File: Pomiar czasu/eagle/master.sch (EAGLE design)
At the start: 36 parts, among them IC1 MEGA8-AI, IC2 lm33, U2 RFM69HW

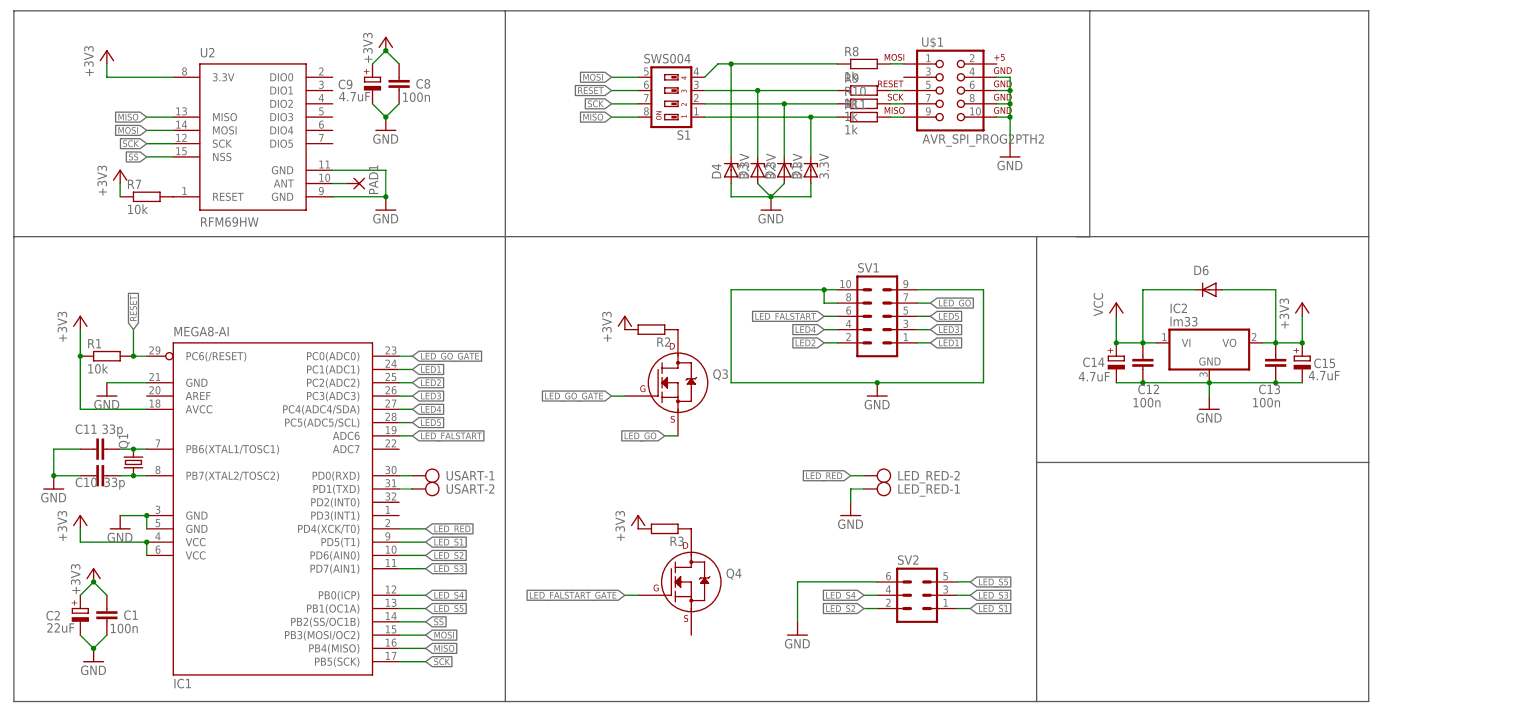
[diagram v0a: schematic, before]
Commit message: ADC slave, master project  created
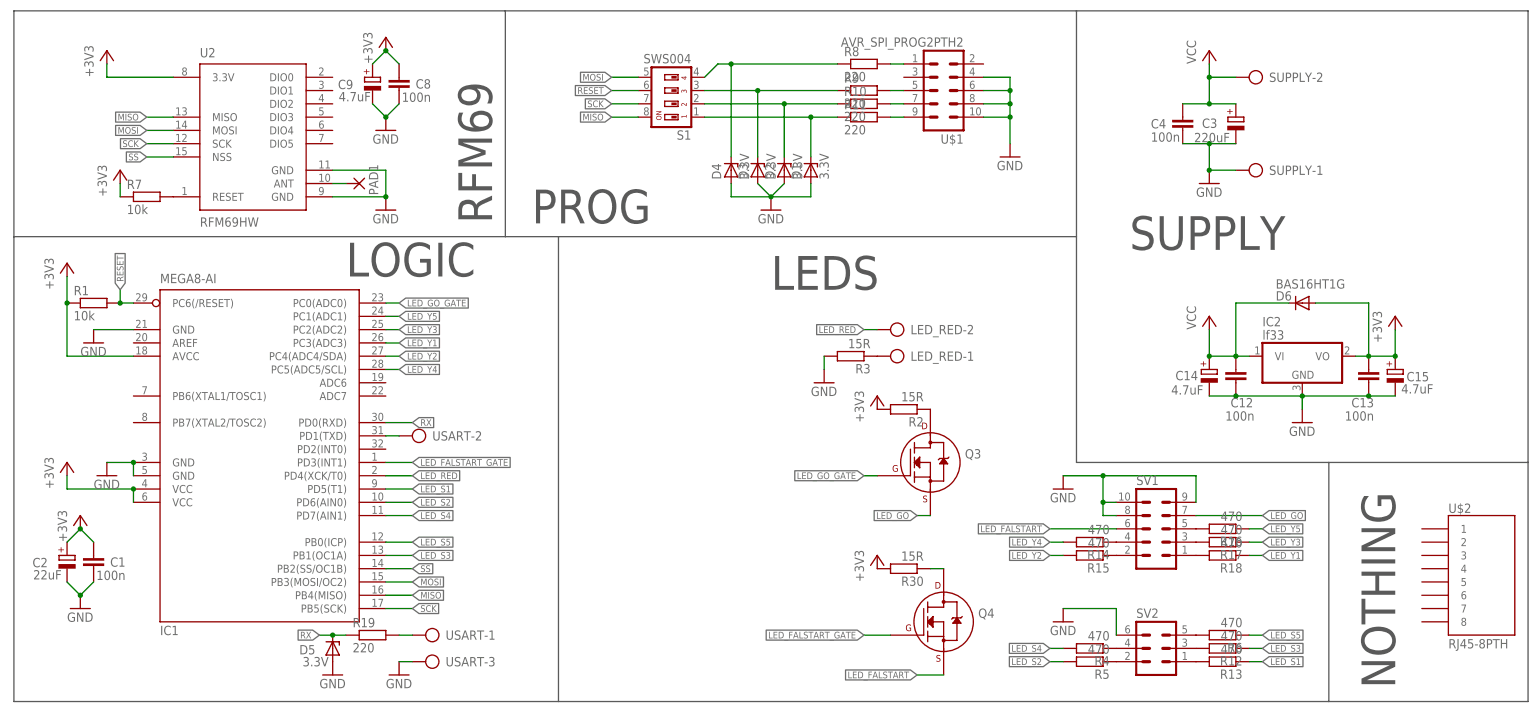
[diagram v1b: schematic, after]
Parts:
- removed C10, C11: 33p, rcl:C-EUC0805
- removed Q1: (no value), crystal:CRYSTALHC49UP
- added C3: 220uF, rcl:CPOL-EUE2-5
- added C4: 100n, rcl:C-EUC0805
- added D5: 3.3V, diode:ZENER-DIODESOD80C
- added R12, R13, R14, R15, R16, R17, R18, R4, R5, R6: 470, rcl:R-EU_R0805
- added R19: 220, rcl:R-EU_R0805
- added R30: 15R, rcl:R-EU_R0805
- added SUPPLY: (no value), con-ptr500:AK500/2
- added U$2: RJ45-8PTH, SparkFun:RJ45-8PTH
- D6: value (none) -> BAS16HT1G
- IC2: value lm33 -> lf33
- R10, R11, R8, R9: value 1k -> 220
- R2, R3: value (none) -> 15R
- U$1: device SparkFun:AVR_SPI_PROG2PTH2 -> con-harting-ml:ML10L
- USART: device con-ptr500:AK500/2 -> con-ptr500:AK500/3
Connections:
- removed net LED1: IC1.PC1(ADC1), SV1.1
- removed net LED2: IC1.PC2(ADC2), SV1.2
- removed net LED3: IC1.PC3(ADC3), SV1.3
- removed net LED4: IC1.PC4(ADC4/SDA), SV1.4
- removed net LED5: IC1.PC5(ADC5/SCL), SV1.5
- removed net N$17: C11.2, IC1.PB6(XTAL1/TOSC1), Q1.2
- removed net N$18: C10.2, IC1.PB7(XTAL2/TOSC2), Q1.1
- removed net RXD: IC1.PD0(RXD), USART-1.KL
- new net LED_Y1: IC1.PC3(ADC3), R18.1
- new net LED_Y2: IC1.PC4(ADC4/SDA), R15.2
- new net LED_Y3: IC1.PC2(ADC2), R17.1
- new net LED_Y4: IC1.PC5(ADC5/SCL), R14.2
- new net LED_Y5: IC1.PC1(ADC1), R16.1
- new net N$19: R12.2, SV2.3
- new net N$20: R13.2, SV2.1
- new net N$21: R14.1, SV1.4
- new net N$22: R15.1, SV1.2
- new net N$23: R16.2, SV1.5
- new net N$24: R17.2, SV1.3
- new net N$25: R18.2, SV1.1
- new net N$26: R19.2, USART-1.KL
- new net N$3: LED_RED-1.KL, R3.1
- new net N$4: R4.1, SV2.4
- new net N$5: R5.1, SV2.2
- new net N$6: R6.2, SV2.5
- new net RX: D5.C, IC1.PD0(RXD), R19.1
- net +3V3: now also R30.2; no longer R3.2
- net GND: now also C3.-, C4.2, D5.A, R3.2, SUPPLY-1.KL, USART-3.KL; no longer C10.1, C11.1, LED_RED-1.KL
- net LED_FALSTART: now also Q4.S; no longer IC1.ADC6
- net LED_FALSTART_GATE: now also IC1.PD3(INT1)
- net LED_S1: now also R13.1; no longer SV2.1
- net LED_S2: now also R5.2; no longer SV2.2
- net LED_S3: now also IC1.PB1(OC1A), R12.1; no longer IC1.PD7(AIN1), SV2.3
- net LED_S4: now also IC1.PD7(AIN1), R4.2; no longer IC1.PB0(ICP), SV2.4
- net LED_S5: now also IC1.PB0(ICP), R6.1; no longer IC1.PB1(OC1A), SV2.5
- net N$2: now also R30.1; no longer R3.1
- net VCC: now also C3.+, C4.1, SUPPLY-2.KL
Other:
- note added: "LEDS"
- note added: "LOGIC"
- note added: "NOTHING"
- note added: "PROG"
- note added: "RFM69"
- note added: "SUPPLY"
- moved on the sheet: C1, C12, C13, C14, C15, C2, D6, IC1, IC2, LED_RED-1, LED_RED-2, Q3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

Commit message: Slave->ctc, tsal modulation
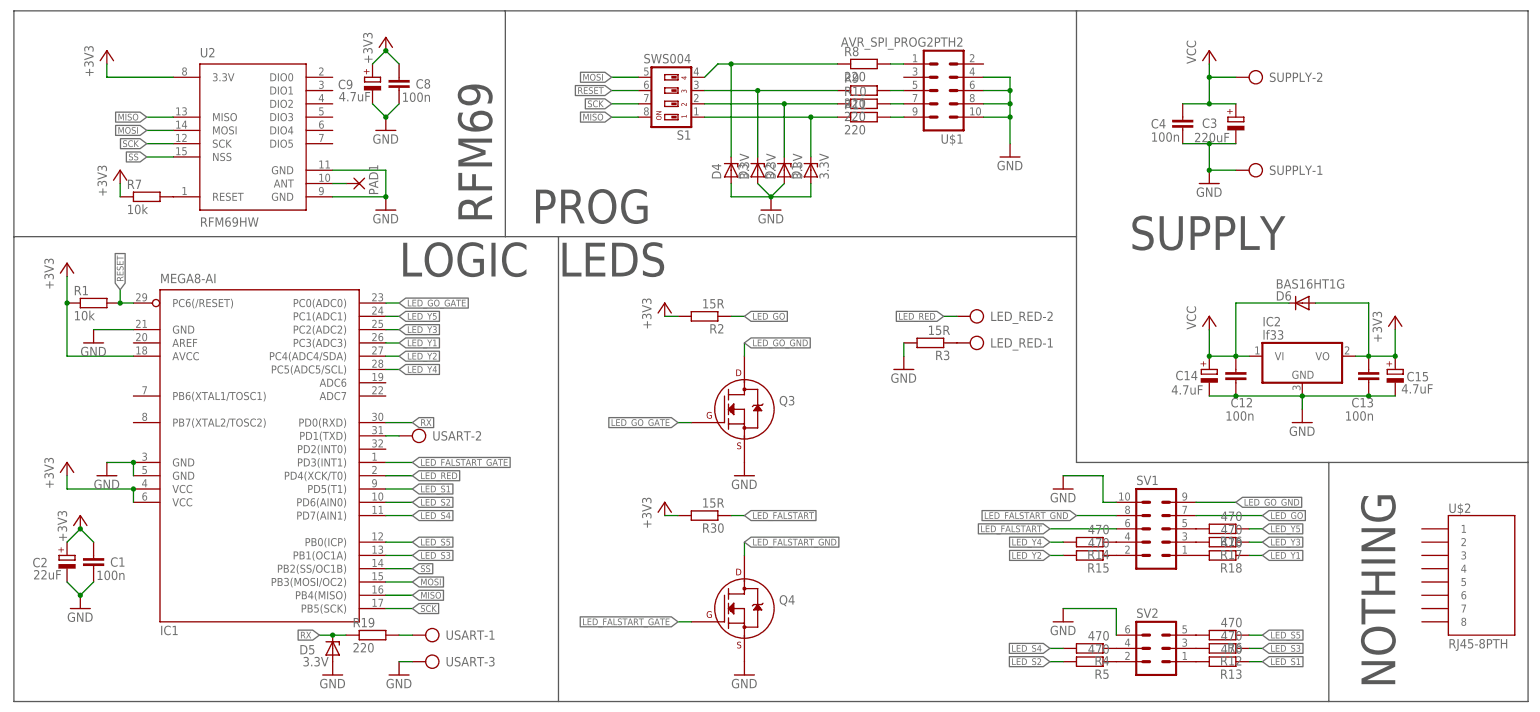
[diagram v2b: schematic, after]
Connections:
- removed net N$1: Q3.D, R2.1
- removed net N$2: Q4.D, R30.1
- new net LED_FALSTART_GND: Q4.D, SV1.8
- new net LED_GO_GND: Q3.D, SV1.9
- net GND: now also Q3.S, Q4.S; no longer SV1.8, SV1.9
- net LED_FALSTART: now also R30.1; no longer Q4.S
- net LED_GO: now also R2.1; no longer Q3.S
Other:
- moved on the sheet: LED_RED-1, LED_RED-2, Q3, Q4, R2, R3, R30
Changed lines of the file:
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@@
 <part name="+3V8" library="supply1" deviceset="+3V3" device=""/>
 <part name="+3V9" library="supply1" deviceset="+3V3" device=""/>
+<part name="GND13" library="supply1" deviceset="GND" device=""/>
+<part name="GND16" library="supply1" deviceset="GND" device=""/>
 </parts>
 <sheets>
@@
 <wire x1="246.38" y1="55.88" x2="198.12" y2="55.88" width="0.1524" layer="97"/>
 <wire x1="246.38" y1="55.88" x2="246.38" y2="10.16" width="0.1524" layer="97"/>
-<text x="139.7" y="88.9" size="6.4516" layer="97">LEDS</text>
-<text x="58.42" y="91.44" size="6.4516" layer="97">LOGIC</text>
+<text x="99.06" y="91.44" size="6.4516" layer="97">LEDS</text>
+<text x="68.58" y="91.44" size="6.4516" layer="97">LOGIC</text>
 <text x="86.36" y="101.6" size="6.4516" layer="97" rot="R90">RFM69</text>
 <text x="93.98" y="101.6" size="6.4516" layer="97">PROG</text>
@@
 <instance part="GND15" gate="1" x="195.58" y="50.8"/>
 <instance part="SV2" gate="1" x="213.36" y="20.32"/>
-<instance part="LED_RED" gate="-1" x="165.1" y="76.2" rot="R180"/>
-<instance part="LED_RED" gate="-2" x="165.1" y="81.28" rot="R180"/>
+<instance part="LED_RED" gate="-1" x="180.34" y="78.74" rot="R180"/>
+<instance part="LED_RED" gate="-2" x="180.34" y="83.82" rot="R180"/>
 <instance part="GND1" gate="1" x="195.58" y="25.4"/>
-<instance part="GND5" gate="1" x="149.86" y="71.12"/>
-<instance part="Q3" gate="G$1" x="170.18" y="55.88"/>
-<instance part="Q4" gate="G$1" x="172.72" y="25.4"/>
-<instance part="R2" gate="G$1" x="165.1" y="66.04" rot="R180"/>
-<instance part="R30" gate="G$1" x="165.1" y="35.56" rot="R180"/>
+<instance part="GND5" gate="1" x="165.1" y="73.66"/>
+<instance part="Q3" gate="G$1" x="134.62" y="66.04"/>
+<instance part="Q4" gate="G$1" x="134.62" y="27.94"/>
+<instance part="R2" gate="G$1" x="127" y="83.82" rot="R180"/>
+<instance part="R30" gate="G$1" x="127" y="45.72" rot="R180"/>
 <instance part="USART" gate="-1" x="76.2" y="22.86" rot="R180"/>
 <instance part="USART" gate="-2" x="73.66" y="60.96" rot="R180"/>
 <instance part="USART" gate="-3" x="76.2" y="17.78" rot="R180"/>
 <instance part="GND6" gate="1" x="68.58" y="15.24"/>
-<instance part="R3" gate="G$1" x="154.94" y="76.2" rot="R180"/>
+<instance part="R3" gate="G$1" x="170.18" y="78.74" rot="R180"/>
 <instance part="R4" gate="G$1" x="200.66" y="20.32" rot="R180"/>
 <instance part="R5" gate="G$1" x="200.66" y="17.78" rot="R180"/>
@@
 <instance part="R19" gate="G$1" x="63.5" y="22.86"/>
 <instance part="GND12" gate="1" x="55.88" y="15.24"/>
-<instance part="+3V8" gate="G$1" x="160.02" y="68.58"/>
-<instance part="+3V9" gate="G$1" x="160.02" y="38.1"/>
+<instance part="+3V8" gate="G$1" x="119.38" y="86.36"/>
+<instance part="+3V9" gate="G$1" x="119.38" y="48.26"/>
+<instance part="GND13" gate="1" x="134.62" y="53.34"/>
+<instance part="GND16" gate="1" x="134.62" y="15.24"/>
 </instances>
 <busses>
@@
 </segment>
 <segment>
-<pinref part="SV1" gate="G$1" pin="8"/>
-<wire x1="205.74" y1="45.72" x2="203.2" y2="45.72" width="0.1524" layer="91"/>
 <pinref part="SV1" gate="G$1" pin="10"/>
 <wire x1="205.74" y1="48.26" x2="203.2" y2="48.26" width="0.1524" layer="91"/>
-<wire x1="203.2" y1="45.72" x2="203.2" y2="48.26" width="0.1524" layer="91"/>
 <pinref part="GND15" gate="1" pin="GND"/>
 <wire x1="203.2" y1="48.26" x2="203.2" y2="53.34" width="0.1524" layer="91"/>
-<junction x="203.2" y="48.26"/>
-<pinref part="SV1" gate="G$1" pin="9"/>
-<wire x1="220.98" y1="48.26" x2="220.98" y2="53.34" width="0.1524" layer="91"/>
 <wire x1="195.58" y1="53.34" x2="203.2" y2="53.34" width="0.1524" layer="91"/>
-<wire x1="203.2" y1="53.34" x2="220.98" y2="53.34" width="0.1524" layer="91"/>
-<junction x="203.2" y="53.34"/>
 </segment>
 <segment>
@@
 <pinref part="R3" gate="G$1" pin="2"/>
 <pinref part="GND5" gate="1" pin="GND"/>
-<wire x1="149.86" y1="76.2" x2="149.86" y2="73.66" width="0.1524" layer="91"/>
+<wire x1="165.1" y1="78.74" x2="165.1" y2="76.2" width="0.1524" layer="91"/>
 </segment>
 <segment>
@@
 <pinref part="D5" gate="G$1" pin="A"/>
 <pinref part="GND12" gate="1" pin="GND"/>
+</segment>
+<segment>
+<pinref part="Q3" gate="G$1" pin="S"/>
+<pinref part="GND13" gate="1" pin="GND"/>
+</segment>
+<segment>
+<pinref part="Q4" gate="G$1" pin="S"/>
+<pinref part="GND16" gate="1" pin="GND"/>
 </segment>
 </net>
@@
 <pinref part="R2" gate="G$1" pin="2"/>
 <pinref part="+3V8" gate="G$1" pin="+3V3"/>
+<wire x1="119.38" y1="83.82" x2="121.92" y2="83.82" width="0.1524" layer="91"/>
 </segment>
 <segment>
 <pinref part="R30" gate="G$1" pin="2"/>
 <pinref part="+3V9" gate="G$1" pin="+3V3"/>
+<wire x1="119.38" y1="45.72" x2="121.92" y2="45.72" width="0.1524" layer="91"/>
 </segment>
 </net>
@@
 </segment>
 <segment>
-<pinref part="Q3" gate="G$1" pin="S"/>
-<wire x1="170.18" y1="45.72" x2="167.64" y2="45.72" width="0.1524" layer="91"/>
-<label x="167.64" y="45.72" size="1.27" layer="95" rot="R180" xref="yes"/>
+<pinref part="R2" gate="G$1" pin="1"/>
+<wire x1="132.08" y1="83.82" x2="134.62" y2="83.82" width="0.1524" layer="91"/>
+<label x="134.62" y="83.82" size="1.27" layer="95" xref="yes"/>
 </segment>
 </net>
@@
 </segment>
 <segment>
-<pinref part="Q4" gate="G$1" pin="S"/>
-<wire x1="172.72" y1="15.24" x2="167.64" y2="15.24" width="0.1524" layer="91"/>
-<label x="167.64" y="15.24" size="1.27" layer="95" rot="R180" xref="yes"/>
+<pinref part="R30" gate="G$1" pin="1"/>
+<wire x1="132.08" y1="45.72" x2="134.62" y2="45.72" width="0.1524" layer="91"/>
+<label x="134.62" y="45.72" size="1.27" layer="95" xref="yes"/>
 </segment>
 </net>
@@
 <segment>
 <pinref part="LED_RED" gate="-2" pin="KL"/>
-<wire x1="160.02" y1="81.28" x2="157.48" y2="81.28" width="0.1524" layer="91"/>
-<label x="157.48" y="81.28" size="1.27" layer="95" rot="R180" xref="yes"/>
+<wire x1="175.26" y1="83.82" x2="172.72" y2="83.82" width="0.1524" layer="91"/>
+<label x="172.72" y="83.82" size="1.27" layer="95" rot="R180" xref="yes"/>
 </segment>
 </net>
@@
 <segment>
 <pinref part="Q3" gate="G$1" pin="G"/>
-<wire x1="160.02" y1="53.34" x2="157.48" y2="53.34" width="0.1524" layer="91"/>
-<label x="157.48" y="53.34" size="1.27" layer="95" rot="R180" xref="yes"/>
+<wire x1="124.46" y1="63.5" x2="121.92" y2="63.5" width="0.1524" layer="91"/>
+<label x="121.92" y="63.5" size="1.27" layer="95" rot="R180" xref="yes"/>
 </segment>
 <segment>
@@
 <segment>
 <pinref part="Q4" gate="G$1" pin="G"/>
-<wire x1="162.56" y1="22.86" x2="157.48" y2="22.86" width="0.1524" layer="91"/>
-<label x="157.48" y="22.86" size="1.27" layer="95" rot="R180" xref="yes"/>
+<wire x1="124.46" y1="25.4" x2="121.92" y2="25.4" width="0.1524" layer="91"/>
+<label x="121.92" y="25.4" size="1.27" layer="95" rot="R180" xref="yes"/>
 </segment>
 <segment>
@@
 <wire x1="66.04" y1="55.88" x2="71.12" y2="55.88" width="0.1524" layer="91"/>
 <label x="71.12" y="55.88" size="1.27" layer="95" xref="yes"/>
-</segment>
-</net>
-<net name="N$1" class="0">
-<segment>
-<pinref part="Q3" gate="G$1" pin="D"/>
-<pinref part="R2" gate="G$1" pin="1"/>
-</segment>
-</net>
-<net name="N$2" class="0">
-<segment>
-<pinref part="Q4" gate="G$1" pin="D"/>
-<pinref part="R30" gate="G$1" pin="1"/>
-<wire x1="172.72" y1="35.56" x2="170.18" y2="35.56" width="0.1524" layer="91"/>
 </segment>
 </net>
@@
 </segment>
 </net>
+<net name="LED_GO_GND" class="0">
+<segment>
+<pinref part="SV1" gate="G$1" pin="9"/>
+<wire x1="220.98" y1="48.26" x2="228.6" y2="48.26" width="0.1524" layer="91"/>
+<label x="228.6" y="48.26" size="1.27" layer="95" xref="yes"/>
+</segment>
+<segment>
+<pinref part="Q3" gate="G$1" pin="D"/>
+<wire x1="134.62" y1="76.2" x2="134.62" y2="78.74" width="0.1524" layer="91"/>
+<label x="134.62" y="78.74" size="1.27" layer="95" xref="yes"/>
+</segment>
+</net>
+<net name="LED_FALSTART_GND" class="0">
+<segment>
+<pinref part="Q4" gate="G$1" pin="D"/>
+<wire x1="134.62" y1="38.1" x2="134.62" y2="40.64" width="0.1524" layer="91"/>
+<label x="134.62" y="40.64" size="1.27" layer="95" xref="yes"/>
+</segment>
+<segment>
+<pinref part="SV1" gate="G$1" pin="8"/>
+<wire x1="205.74" y1="45.72" x2="198.12" y2="45.72" width="0.1524" layer="91"/>
+<label x="198.12" y="45.72" size="1.27" layer="95" rot="R180" xref="yes"/>
+</segment>
+</net>

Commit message: RFM69:communication master->sensor works!
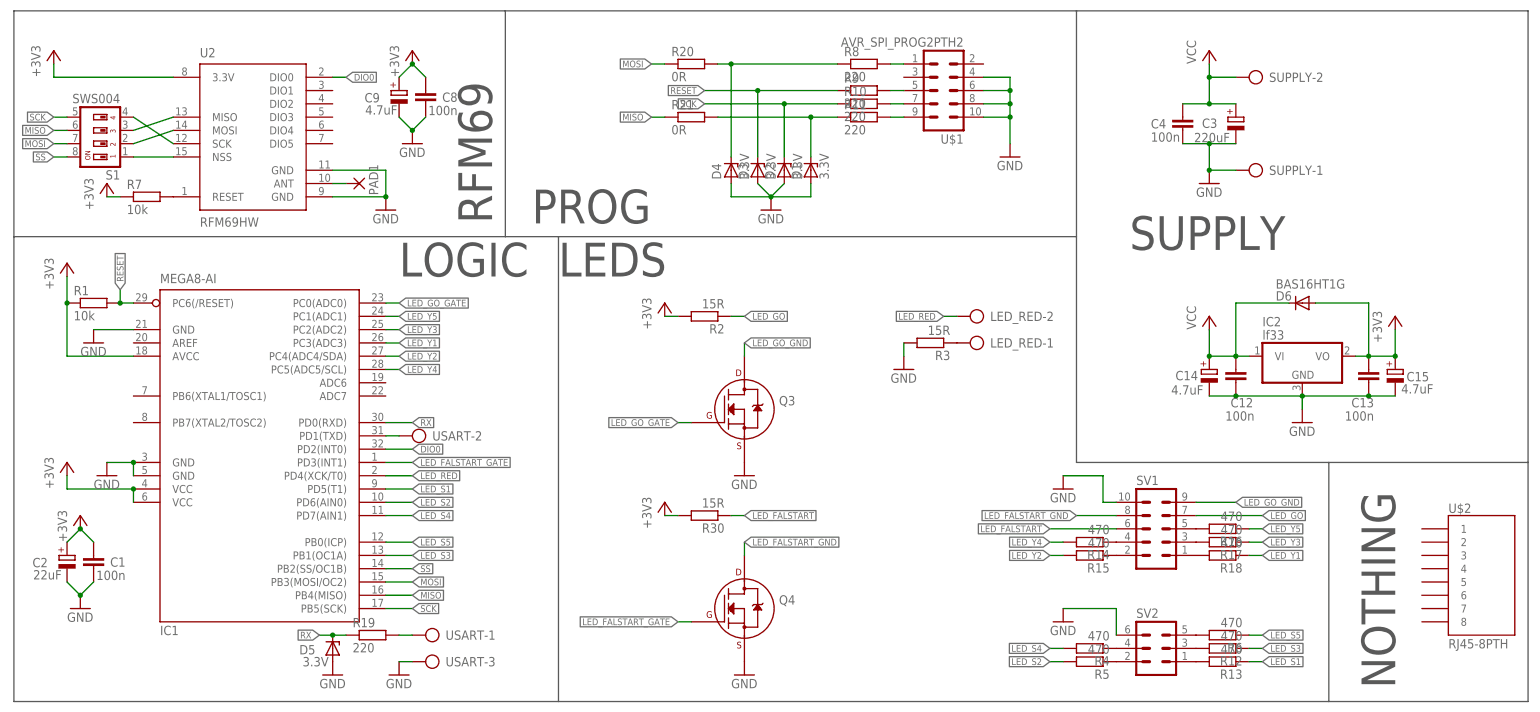
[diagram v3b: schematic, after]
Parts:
- added R20, R21: 0R, rcl:R-EU_R1206
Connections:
- new net DIO0: IC1.PD2(INT0), U2.DIO0
- new net N$1: D1.C, R11.1, R21.2
- new net N$2: D4.C, R20.2, R8.1
- net MISO: now also R21.1, S1.6; no longer S1.8, U2.MISO
- net MOSI: now also R20.1, S1.7; no longer S1.5, U2.MOSI
- net N$10: now also S1.4, U2.SCK; no longer D3.C, R9.1, S1.3
- net N$11: now also S1.3, U2.MISO; no longer D2.C, R10.1, S1.2
- net N$12: now also S1.2, U2.MOSI; no longer D1.C, R11.1, S1.1
- net N$8: now also S1.1, U2.NSS; no longer D4.C, R8.1, S1.4
- net RESET: now also D3.C, R9.1; no longer S1.6
- net SCK: now also D2.C, R10.1, S1.5; no longer S1.7, U2.SCK
- net SS: now also S1.8; no longer U2.NSS
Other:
- moved on the sheet: C8, C9, S1
